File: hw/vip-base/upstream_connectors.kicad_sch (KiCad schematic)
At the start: 2 parts, among them J2 Conn_02x30_Odd_Even, J3 Conn_02x30_Odd_Even

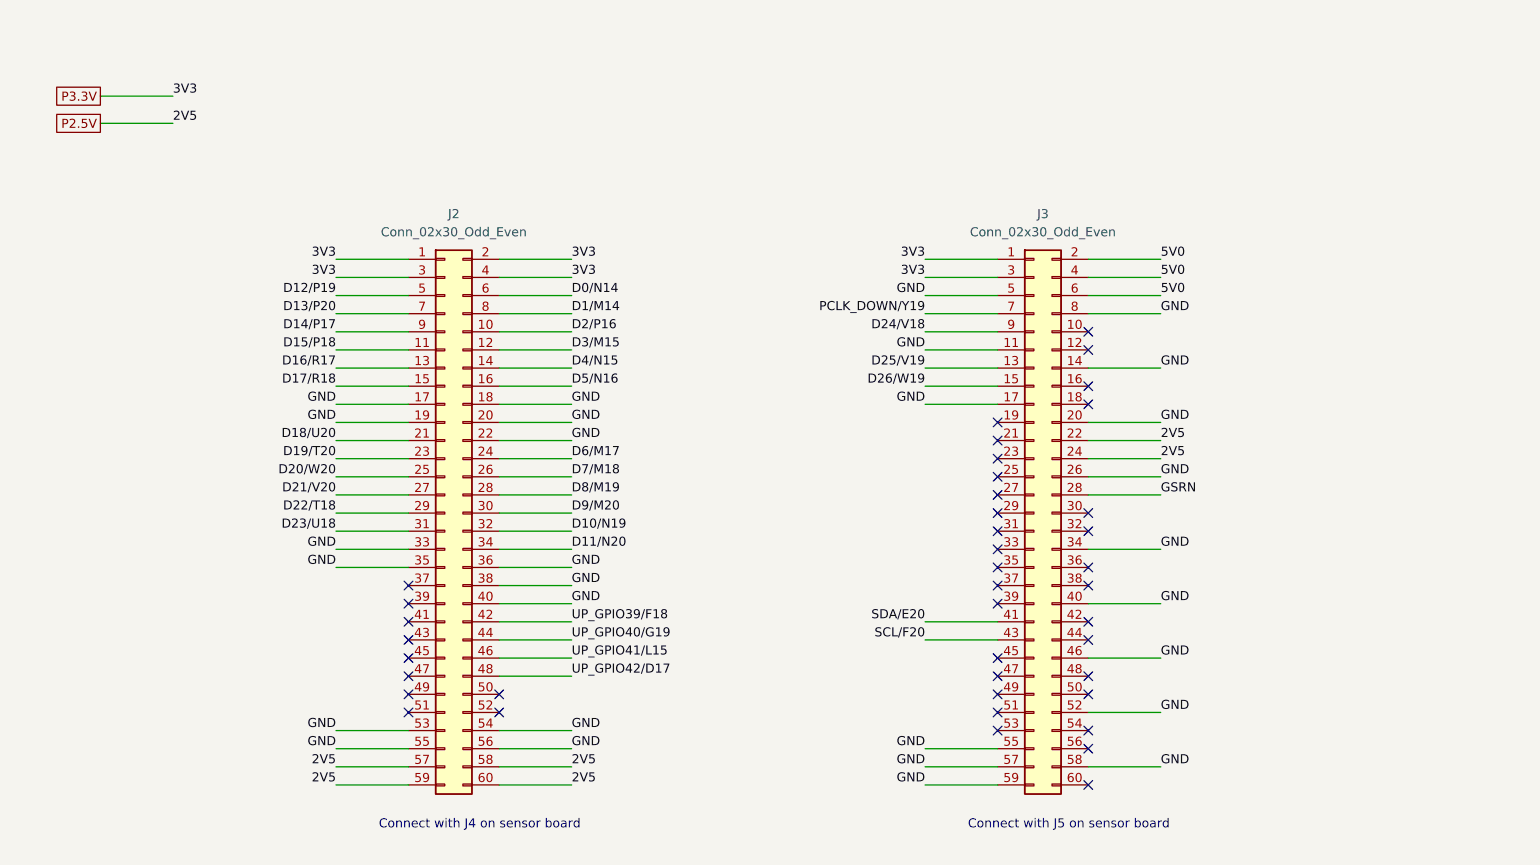
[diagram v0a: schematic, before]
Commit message: hw: Finish main routing
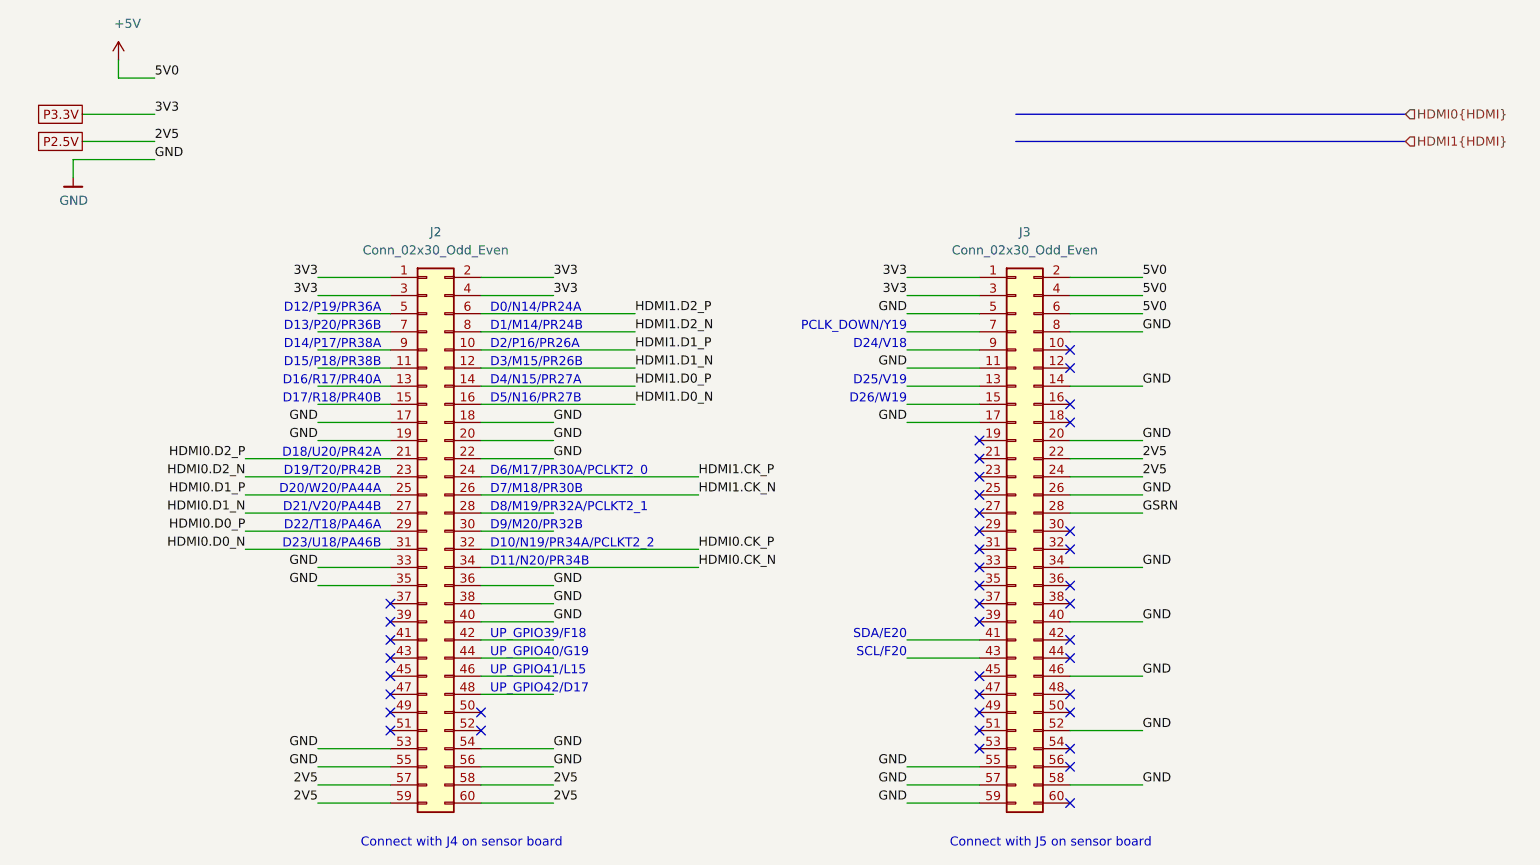
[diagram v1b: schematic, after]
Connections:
- net 5V0 renamed +5V
- net D0/N14 renamed HDMI1.D2_P
- net D10/N19 renamed HDMI0.CK_P
- net D11/N20 renamed HDMI0.CK_N
- net D12/P19: no longer names the net of J2.5 (Pin_5)
- net D13/P20: no longer names the net of J2.7 (Pin_7)
- net D14/P17: no longer names the net of J2.9 (Pin_9)
- net D15/P18: no longer names the net of J2.11 (Pin_11)
- net D16/R17: no longer names the net of J2.13 (Pin_13)
- net D17/R18: no longer names the net of J2.15 (Pin_15)
- net D18/U20 renamed HDMI0.D2_P
- net D19/T20 renamed HDMI0.D2_N
- net D1/M14 renamed HDMI1.D2_N
- net D20/W20 renamed HDMI0.D1_P
- net D21/V20 renamed HDMI0.D1_N
- net D22/T18 renamed HDMI0.D0_P
- net D23/U18 renamed HDMI0.D0_N
- net D24/V18: no longer names the net of J3.9 (Pin_9)
- net D25/V19: no longer names the net of J3.13 (Pin_13)
- net D26/W19: no longer names the net of J3.15 (Pin_15)
- net D2/P16 renamed HDMI1.D1_P
- net D3/M15 renamed HDMI1.D1_N
- net D4/N15 renamed HDMI1.D0_P
- net D5/N16 renamed HDMI1.D0_N
- net D6/M17 renamed HDMI1.CK_P
- net D7/M18 renamed HDMI1.CK_N
- net D8/M19: no longer names the net of J2.28 (Pin_28)
- net D9/M20: no longer names the net of J2.30 (Pin_30)
- net PCLK_DOWN/Y19: no longer names the net of J3.7 (Pin_7)
- net SCL/F20: no longer names the net of J3.43 (Pin_43)
- net SDA/E20: no longer names the net of J3.41 (Pin_41)
- net UP_GPIO39/F18: no longer names the net of J2.42 (Pin_42)
- net UP_GPIO40/G19: no longer names the net of J2.44 (Pin_44)
- net UP_GPIO41/L15: no longer names the net of J2.46 (Pin_46)
- net UP_GPIO42/D17: no longer names the net of J2.48 (Pin_48)
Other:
- note added: "D0/N14/PR24A"
- note added: "D1/M14/PR24B"
- note added: "D10/N19/PR34A/PCLKT2_2"
- note added: "D11/N20/PR34B"
- note added: "D12/P19/PR36A"
- note added: "D13/P20/PR36B"
- note added: "D14/P17/PR38A"
- note added: "D15/P18/PR38B"
- note added: "D16/R17/PR40A"
- note added: "D17/R18/PR40B"
- note added: "D18/U20/PR42A"
- note added: "D19/T20/PR42B"
- note added: "D2/P16/PR26A"
- note added: "D20/W20/PA44A"
- note added: "D21/V20/PA44B"
- note added: "D22/T18/PA46A"
- note added: "D23/U18/PA46B"
- note added: "D24/V18"
- note added: "D25/V19"
- note added: "D26/W19"
- note added: "D3/M15/PR26B"
- note added: "D4/N15/PR27A"
- note added: "D5/N16/PR27B"
- note added: "D6/M17/PR30A/PCLKT2_0"
- note added: "D7/M18/PR30B"
- note added: "D8/M19/PR32A/PCLKT2_1"
- note added: "D9/M20/PR32B"
- note added: "PCLK_DOWN/Y19"
- note added: "SCL/F20"
- note added: "SDA/E20"
- note added: "UP_GPIO39/F18"
- note added: "UP_GPIO40/G19"
- note added: "UP_GPIO41/L15"
- note added: "UP_GPIO42/D17"
- company: (none) -> GsD
- title: (none) -> VIP Base
- moved on the sheet: J2, J3
